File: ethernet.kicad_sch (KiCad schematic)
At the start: 51 parts

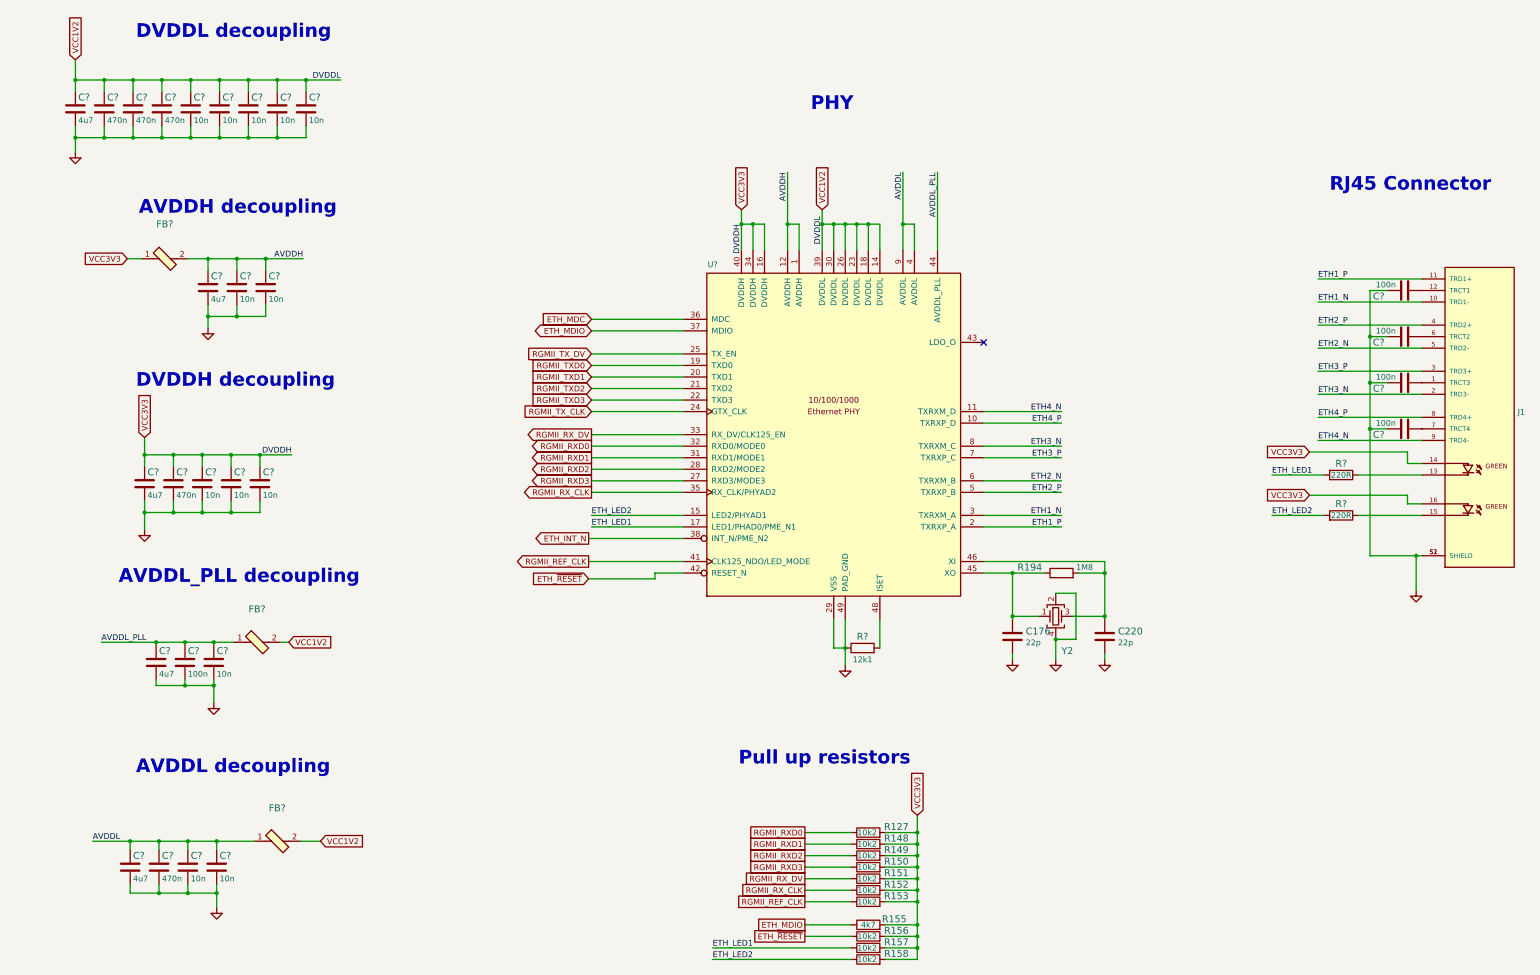
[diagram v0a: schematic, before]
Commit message: Introduce component standardization
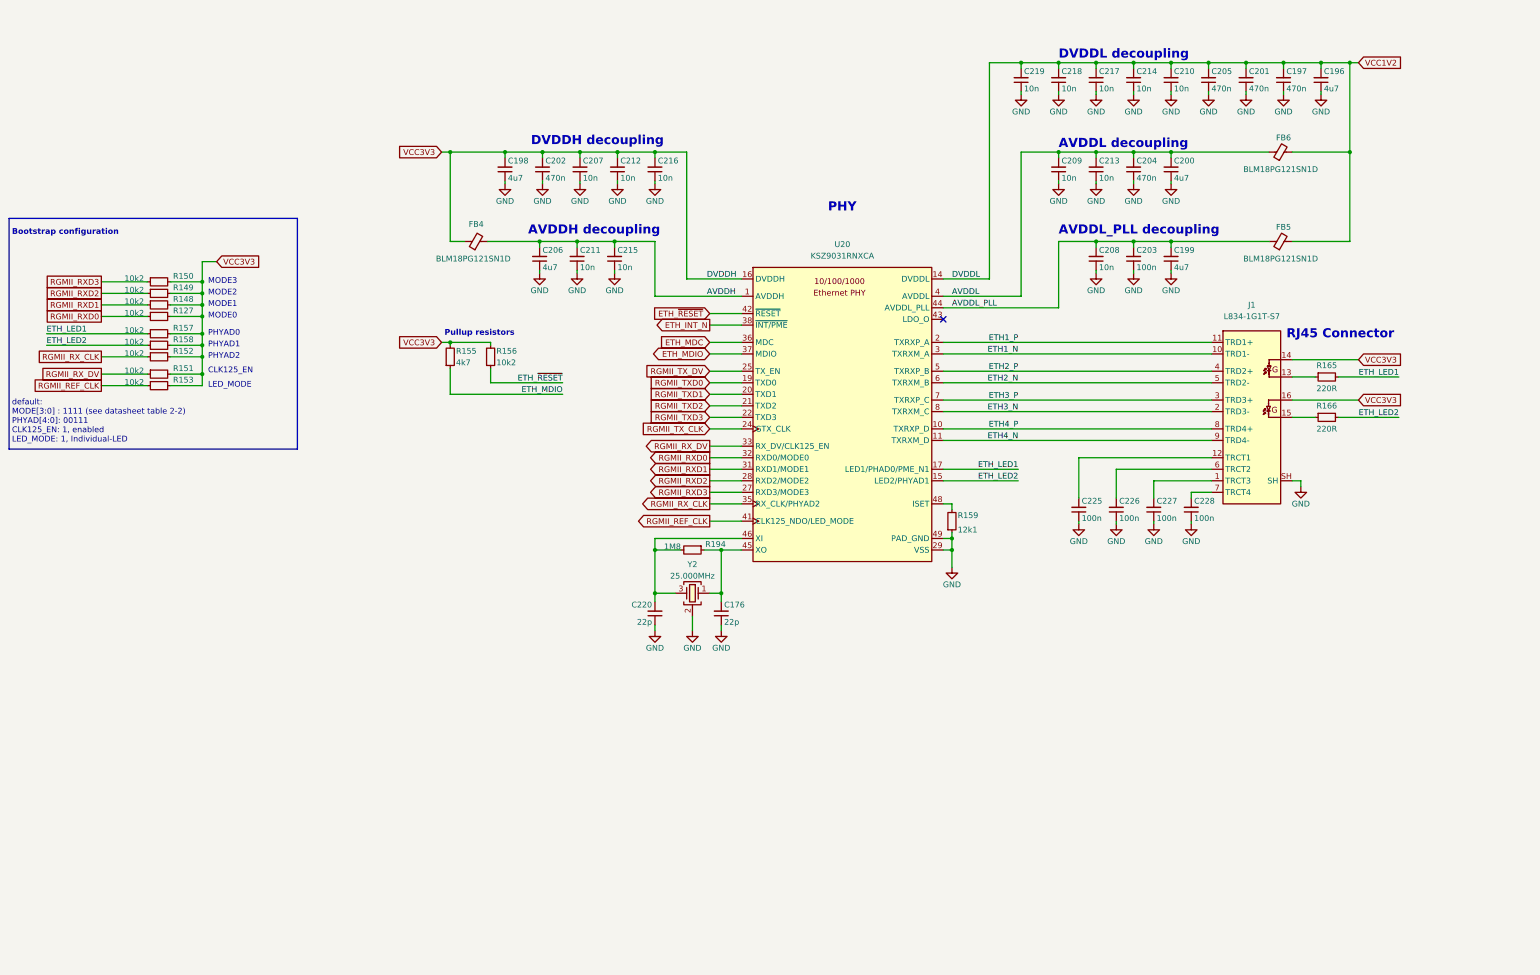
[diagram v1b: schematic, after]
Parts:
- C176, C220: value (none) -> C_22p_0402; footprint (none) -> antmicro-footprints:C_0402_1005Metric; symbol artix-dc-scm:C_22p_0402 -> antmicroCapacitors0402:C_22p_0402; Author (none) -> Antmicro; License (none) -> Apache-2.0; Manufacturer YAGEO -> Yaego
- C196, C198, C199, C200, C206: renamed from C?; value (none) -> C_4u7_0402; footprint (none) -> antmicro-footprints:C_0402_1005Metric; symbol artix-dc-scm:C_4u7_0402 -> antmicroCapacitors0402:C_4u7_0402; Author (none) -> Antmicro; License (none) -> Apache-2.0; Manufacturer MURATA -> Murata
- C197, C201, C202, C204, C205: renamed from C?; value (none) -> C_470n_0402; footprint (none) -> antmicro-footprints:C_0402_1005Metric; symbol artix-dc-scm:C_470n_0402 -> antmicroCapacitors0402:C_470n_0402; Author (none) -> Antmicro; License (none) -> Apache-2.0
- C203, C225, C226, C227, C228: renamed from C?; value (none) -> C_100n_0402; footprint (none) -> antmicro-footprints:C_0402_1005Metric; symbol artix-dc-scm:C_100n_0402 -> antmicroCapacitors0402:C_100n_0402; Author (none) -> Antmicro; Dielectric (none) -> X5R; License (none) -> Apache-2.0; MPN 0402X104K6R3CT -> GRM155R61H104KE14D; Manufacturer Walsin -> Murata; Voltage (none) -> 50V
- C207, C208, C209, C210, C211, C212, C213, C214, C215, C216, C217, C218, C219: renamed from C?; value (none) -> C_10n_0402; footprint (none) -> antmicro-footprints:C_0402_1005Metric; symbol artix-dc-scm:C_10n_0402 -> antmicroCapacitors0402:C_10n_0402; Author (none) -> Antmicro; Dielectric (none) -> X7R; License (none) -> Apache-2.0; MPN 04025G103ZAT2A -> GRM155R71H103KA88D; Manufacturer AVX -> Murata; Voltage (none) -> 50V
- FB4, FB5, FB6: renamed from FB?; value (none) -> FB_120Z_2A_0603; footprint (none) -> antmicro-footprints:FB_0603_1608Metric; symbol artix-dc-scm:BLM18PG121SN1D -> antmicroFerriteBeadsandChips:FB_120Z_2A_0603; Author (none) -> Antmicro; License (none) -> Apache-2.0; Manufacturer Murata Electronics North America -> Murata
- J1: value (none) -> L834-1G1T-S7; footprint (none) -> antmicro-footprints:RJ45_BEL_L834-1G1T-S7; symbol artix-dc-scm:L834-1G1T-S7 -> antmicroModularConnectorsJacksWithMagnetics:L834-1G1T-S7; Author (none) -> Antmicro; License (none) -> Apache-2.0
- R127, R148, R149, R150, R151, R152, R153, R156, R157, R158: value (none) -> R_10k2_0402; footprint (none) -> antmicro-footprints:R_0402_1005Metric; symbol artix-dc-scm:R_10k2_0402 -> antmicroResistors0402:R_10k2_0402; Author (none) -> Antmicro; License (none) -> Apache-2.0; MPN MCWR04X1022FTL -> CR0402-FX-1022GLF; Manufacturer MULTICOMP PRO -> Bourns; Tolerance (none) -> 1%
- R155: value (none) -> R_4k7_0402; footprint (none) -> antmicro-footprints:R_0402_1005Metric; symbol artix-dc-scm:R_4k7_0402 -> antmicroResistors0402:R_4k7_0402; Author (none) -> Antmicro; License (none) -> Apache-2.0; MPN ERJ2GEJ472X -> CR0402-FX-4701GLF; Manufacturer PANASONIC_ELECTRONIC_COMPONENTS -> Bourns; Tolerance (none) -> 1%
- R159: renamed from R?; value (none) -> R_12k1_0402; footprint (none) -> antmicro-footprints:R_0402_1005Metric; symbol artix-dc-scm:R_12k1_0402 -> antmicroResistors0402:R_12k1_0402; Author (none) -> Antmicro; License (none) -> Apache-2.0; MPN MCWR04X1212FTL -> CR0402-FX-1212GLF; Manufacturer MULTICOMP -> Bourns; Tolerance (none) -> 1%
- R165, R166: renamed from R?; value (none) -> R_220R_0402; footprint (none) -> antmicro-footprints:R_0402_1005Metric; symbol artix-dc-scm:R_220R_0402 -> antmicroResistors0402:R_220R_0402; Author (none) -> Antmicro; License (none) -> Apache-2.0; MPN ERJ2GEJ221X -> CR0402-FX-2200GLF; Manufacturer Panasonic -> Bourns; Tolerance (none) -> 1%
- R194: value (none) -> R_1M8_0402; footprint (none) -> antmicro-footprints:R_0402_1005Metric; symbol artix-dc-scm:R_1M8_0402 -> antmicroResistors0402:R_1M8_0402; Author (none) -> Antmicro; License (none) -> Apache-2.0; MPN MCMR04X185_JTL -> CR0402-FX-1804GLF; Manufacturer MULTICOMP -> Bourns; Tolerance (none) -> 1%
- U20: renamed from U?; value (none) -> KSZ9031RNXCA; footprint (none) -> antmicro-footprints:QFN-48-1EP_7x7x0.9mm_P0.5mm_EP5x5mm; symbol artix-dc-scm:KSZ9031RNXCA -> antmicroInterfaceControllers:KSZ9031RNXCA; Author (none) -> Antmicro; License (none) -> Apache-2.0
- Y2: value (none) -> ABM8G-25.000MHZ-18-D2Y-T3; footprint (none) -> antmicro-footprints:Oscillator_SMD_Geyer_KX-7-4Pin_3.2x2.5mm; symbol artix-dc-scm:ABM8G-25.000MHZ-18-D2Y-T -> antmicroCrystals:ABM8G-25.000MHZ-18-D2Y-T3; Author (none) -> Antmicro; License (none) -> Apache-2.0; MPN ABM8G-25.000MHZ-18-D2Y-T -> ABM8G-25.000MHZ-18-D2Y-T3; Val (none) -> 25.000MHz
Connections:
- net AVDDH: now also C206.2, C211.2, C215.2; no longer C206.1, C211.1, C215.1
- net AVDDL: now also C200.2, C204.2, C209.2, C213.2; no longer C200.1, C204.1, C209.1, C213.1
- net AVDDL_PLL: now also C199.2, C203.2, C208.2; no longer C199.1, C203.1, C208.1
- net GND: now also C176.1, C196.1, C197.1, C198.1, C199.1, C200.1, C201.1, C202.1, C203.1, C204.1, C205.1, C206.1, C207.1, C208.1, C209.1, C210.1, C211.1, C212.1, C213.1, C214.1, C215.1, C216.1, C217.1, C218.1, C219.1, C220.1, C225.1, C226.1, C227.1, C228.1, J1.SH; no longer C176.2, C196.2, C197.2, C198.2, C199.2, C200.2, C201.2, C202.2, C203.2, C204.2, C205.2, C206.2, C207.2, C208.2, C209.2, C210.2, C211.2, C212.2, C213.2, C214.2, C215.2, C216.2, C217.2, C218.2, C219.2, C220.2, C225.2, C226.2, C227.2, C228.2, J1.S1 (SHIELD), J1.S2 (SHIELD)
- net VCC1V2: now also C196.2, C197.2, C201.2, C205.2, C210.2, C214.2, C217.2, C218.2, C219.2; no longer C196.1, C197.1, C201.1, C205.1, C210.1, C214.1, C217.1, C218.1, C219.1
- net VCC3V3: now also C198.2, C202.2, C207.2, C212.2, C216.2; no longer C198.1, C202.1, C207.1, C212.1, C216.1
- net at U20.13 (NC): now also U20.47 (NC)
- net at R194.1, U20.45 (XO), Y2.1: now also C176.2; no longer C176.1
- net at R194.2, U20.46 (XI), Y2.3: now also C220.2; no longer C220.1
- net at J1.1 (TRCT3): now also C227.2; no longer C227.1
- net at J1.12 (TRCT1): now also C225.2; no longer C225.1
- net at J1.6 (TRCT2): now also C226.2; no longer C226.1
- net at J1.7 (TRCT4): now also C228.2; no longer C228.1
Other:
- note added: "Bootstrap configuration"
- note added: "CLK125_EN"
- note added: "LED_MODE"
- note added: "MODE0"
- note added: "MODE1"
- note added: "MODE2"
- note added: "MODE3"
- note added: "PHYAD0"
- note added: "PHYAD1"
- note added: "PHYAD2"
- note added: "Pullup resistors"
- note added: "default: MODE[3:0] : 1111 (see datasheet table 2-2) PHYAD[4:0]: 00111 CLK125_EN: 1, enabled LED_MODE: 1, Individual-LED"
- note removed: "Pull up resistors"
- moved on the sheet: C176, C196, C197, C198, C199, C200, C201, C202, C203, C204, C205, C206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

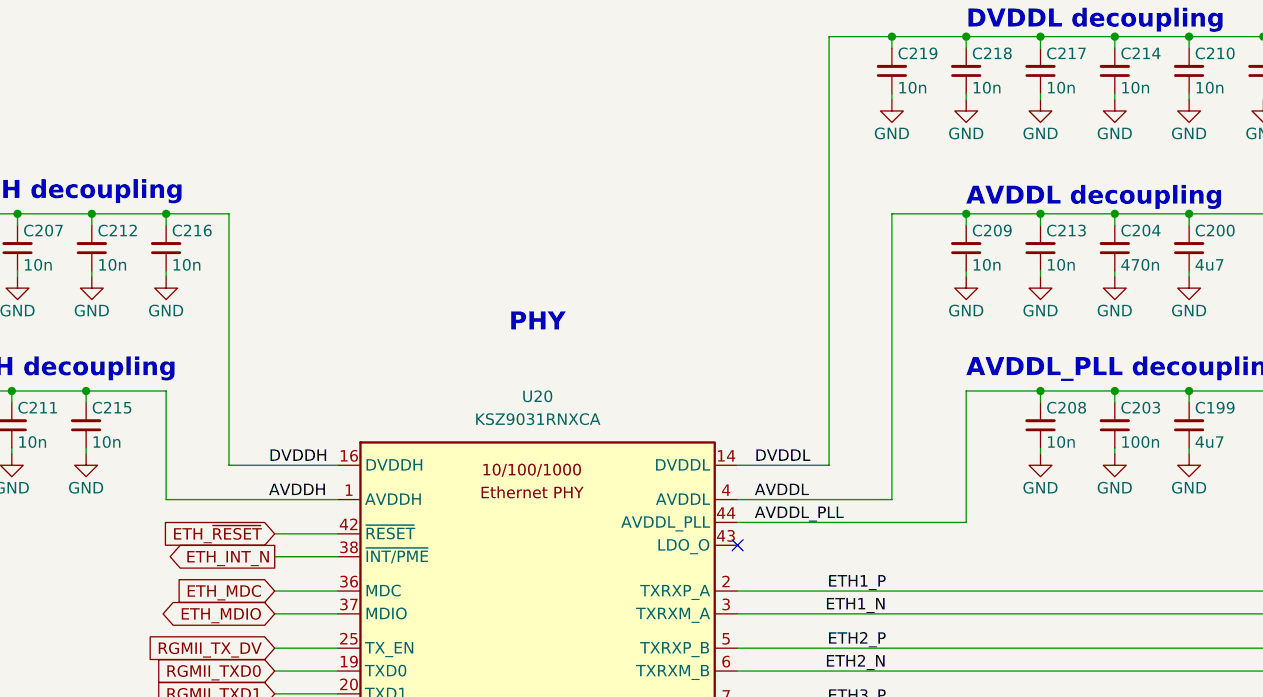
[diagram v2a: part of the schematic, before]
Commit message: Fix schematic ERC errors. ERC clean
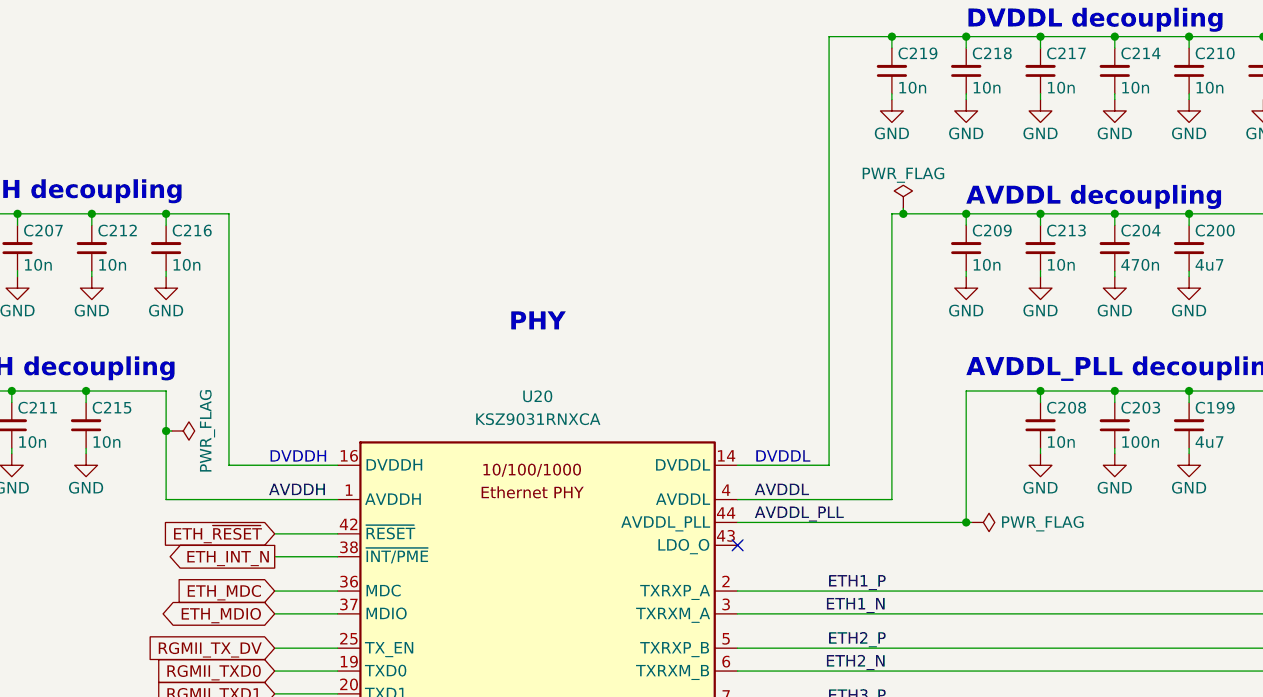
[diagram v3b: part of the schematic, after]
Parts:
- U20: footprint antmicro-footprints:QFN-48-1EP_7x7x0.9mm_P0.5mm_EP5x5mm -> antmicro-footprints:QFN-48-1EP_7x7x0.9mm_P0.5mm_EP3.5x3.5mm
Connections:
- net at U20.13 (NC): no longer U20.47 (NC)
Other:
- note added: "DVDDH"
- note added: "DVDDL"
